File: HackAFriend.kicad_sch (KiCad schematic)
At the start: 8 parts

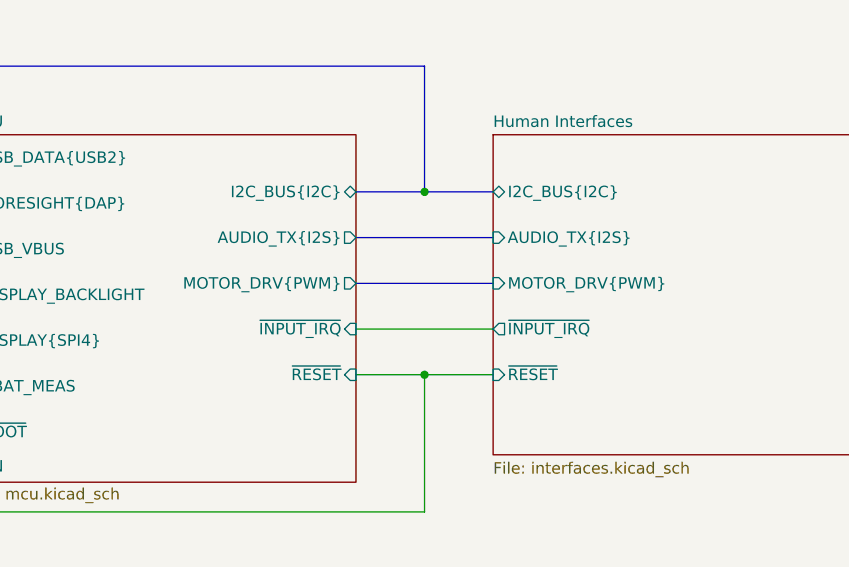
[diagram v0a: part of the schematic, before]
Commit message: Replaced DA7280 with DRV2605
Replaced DA7280 with DRV2605 to simplify board support code in Hack-A-Friend Arduino Library.
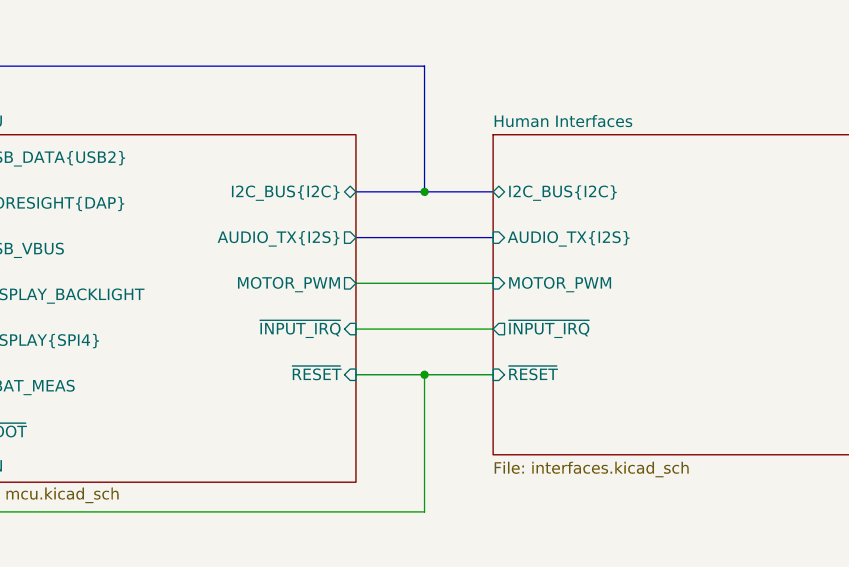
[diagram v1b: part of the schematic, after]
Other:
- sheet Human Interfaces ports: added MOTOR_PWM; removed MOTOR_DRV{PWM}
- sheet MCU ports: added MOTOR_PWM; removed MOTOR_DRV{PWM}
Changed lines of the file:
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@@
+		)
+	)
+	(wire
+		(pts
+			(xy 173.99 69.85) (xy 189.23 69.85)
+		)
+		(stroke
+			(width 0)
+			(type default)
 		)
 	)
@@
 		(pts
 			(xy 113.03 95.25) (xy 121.92 95.25)
-		)
-		(stroke
-			(width 0)
-			(type default)
-		)
-	)
-	(bus
-		(pts
-			(xy 173.99 69.85) (xy 189.23 69.85)
 		)
 		(stroke
@@
 			)
 		)
-		(pin "MOTOR_DRV{PWM}" output
-			(at 173.99 69.85 0)
-			(effects
-				(font
-					(size 1.27 1.27)
-				)
-				(justify right)
-			)
-		)
 		(pin "~{INPUT_IRQ}" input
 			(at 173.99 74.93 0)
@@
 				)
 				(justify left)
+			)
+		)
+		(pin "MOTOR_PWM" output
+			(at 173.99 69.85 0)
+			(effects
+				(font
+					(size 1.27 1.27)
+				)
+				(justify right)
 			)
 		)
@@
 			)
 		)
-		(pin "MOTOR_DRV{PWM}" input
-			(at 189.23 69.85 180)
-			(effects
-				(font
-					(size 1.27 1.27)
-				)
-				(justify left)
-			)
-		)
 		(pin "~{INPUT_IRQ}" output
 			(at 189.23 74.93 180)
 			(effects
 				(font
+					(size 1.27 1.27)
+				)
+				(justify left)
+			)
+		)
+		(pin "MOTOR_PWM" input
+			(at 189.23 69.85 180)
+			(effects
+				(font
